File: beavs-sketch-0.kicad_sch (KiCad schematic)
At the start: 16 parts, among them J1 USB_C_Receptacle_USB2.0_16P, J5 Conn_01x02, U15 SN74LVC4245APW, U16 SRV05-4, U17 SRV05-4

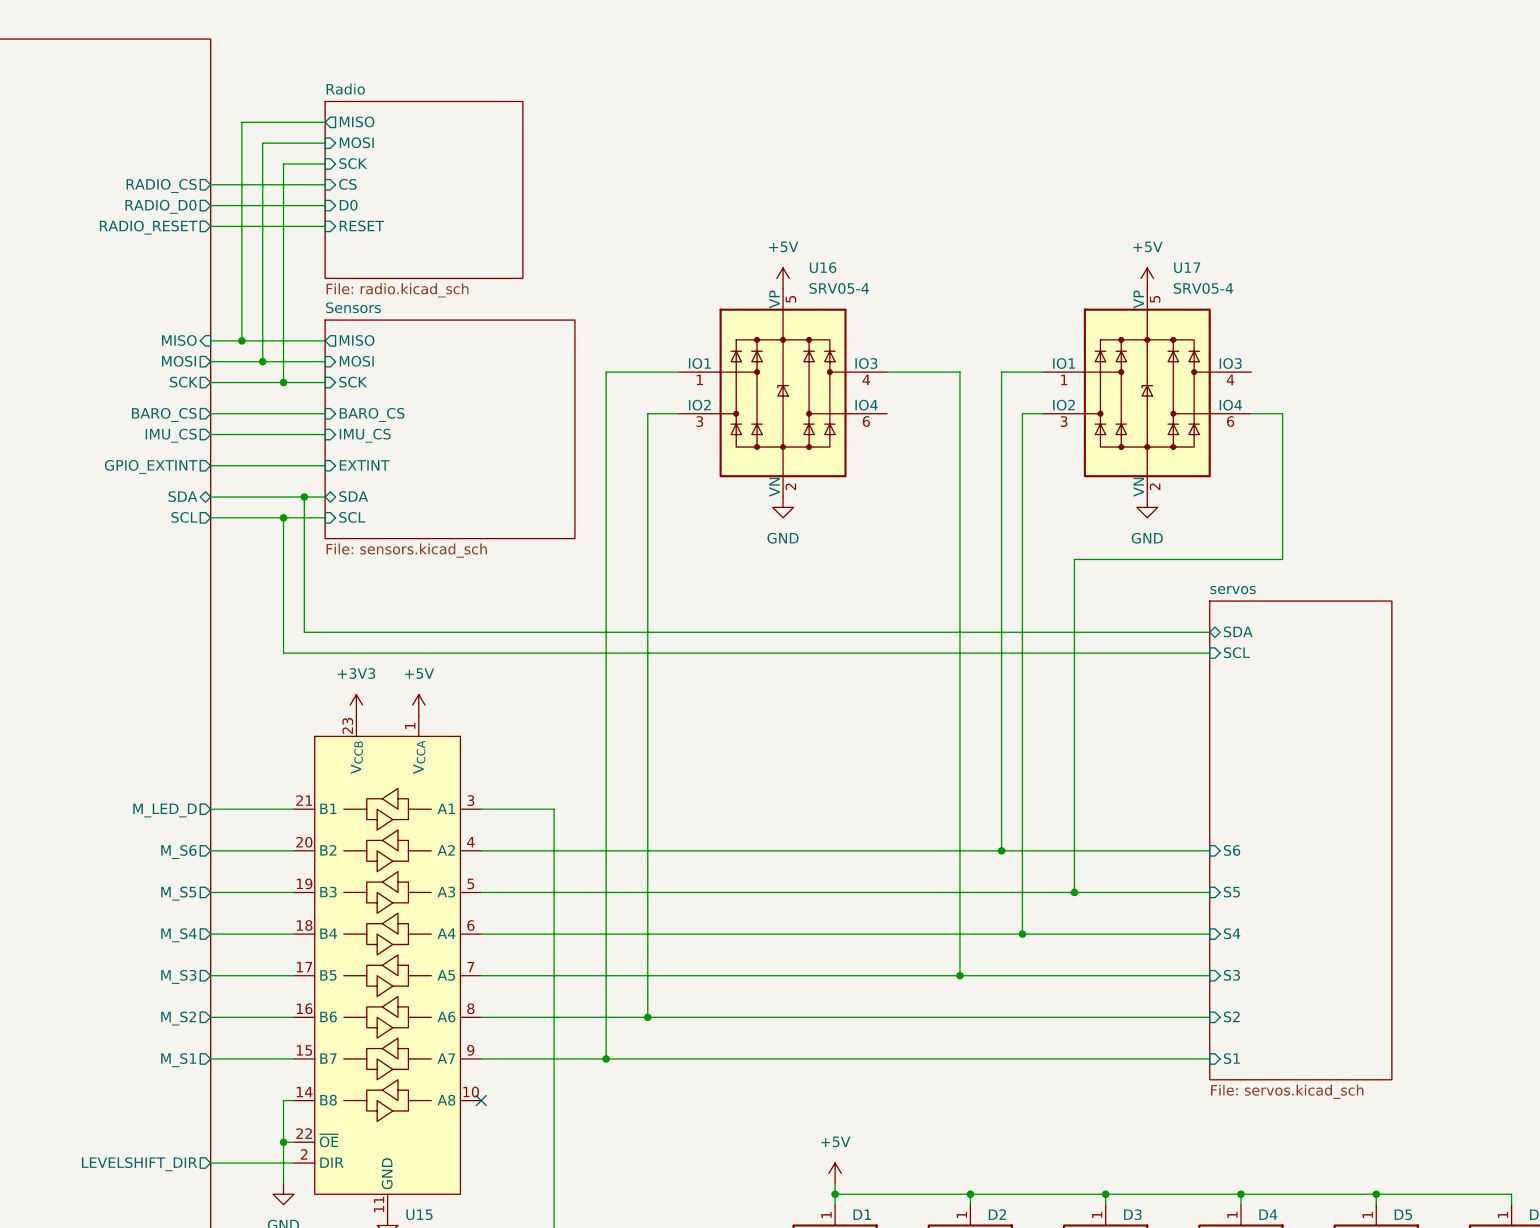
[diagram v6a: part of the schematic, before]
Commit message: switched to global labels for SPI and I2C, added labels for servos
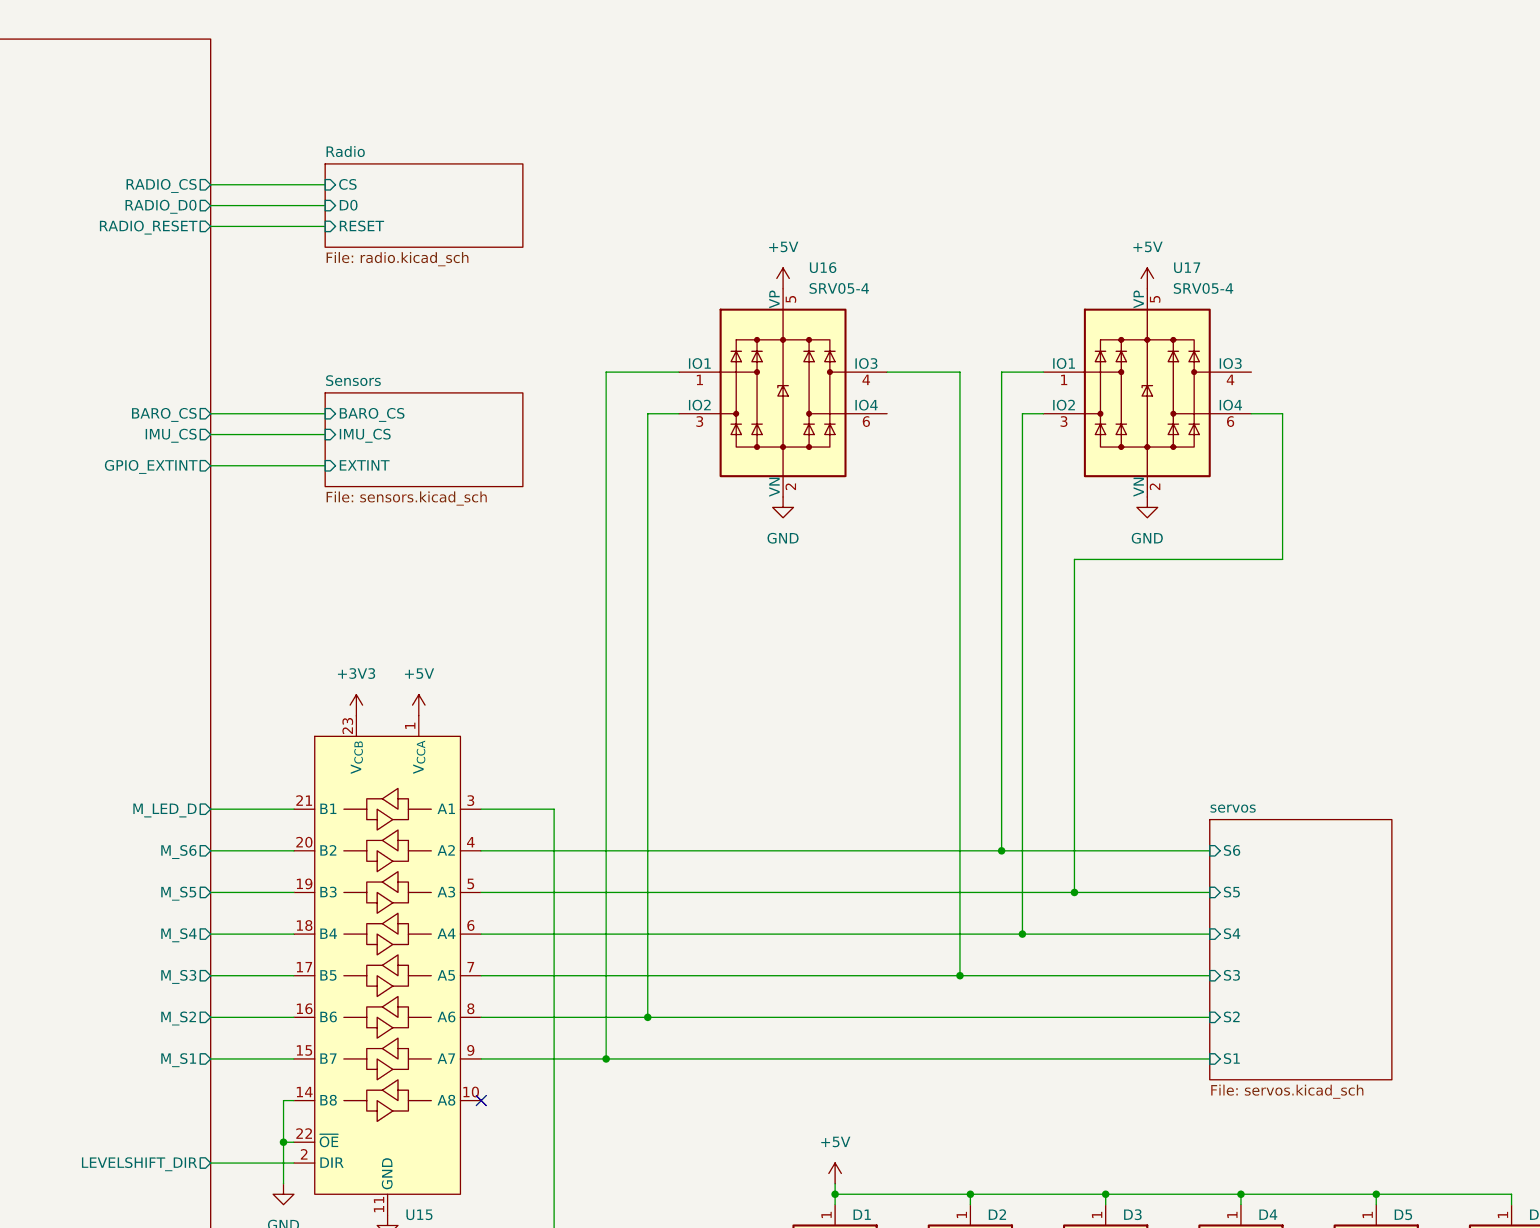
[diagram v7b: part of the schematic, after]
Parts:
- U15: LCSC (none) -> C7859
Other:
- sheet Radio ports: added none; removed MISO, MOSI, SCK
- sheet Sensors ports: added none; removed MISO, MOSI, SCK, SCL, SDA
- sheet mcu ports: added none; removed MISO, MOSI, SCK, SCL, SDA
- sheet servos ports: added none; removed SCL, SDA
